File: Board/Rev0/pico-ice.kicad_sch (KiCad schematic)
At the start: 106 parts, among them J1 USB_C_Receptacle_USB2.0, J10 2x3_2.54mm_Female, J11 2x3_2.54mm_Female, J3 6X2 Female Header, J4 6X2 Female Header, J5 Conn_ARM_JTAG_SWD_10, J6 6X2 Female Header, J7 6X2 Female Header, J8 6X2 Female Header, J9 BOOT_SEL, SW1 PTS820 J25K SMTR LFS, SW2 PTS820 J25K SMTR LFS, U1 NCP1117ST33T3G, U2 W25Q32JVSSIQ, U3 RP2040, U4 CL9293A12L5M, U5 APS6404L-3SQN-SN, U6 ICE40UP5K-SG48ITR, U8 W25Q32JVSSIQ, Y1 12 MHz

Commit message: Updated the silkscreen layer
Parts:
- added LOGO1: tinyVS Logo, CUSTOM:tinyAI_logo, symbol MK11_PROG-rescue:TestPoint_Small-custom
- added LOGO2: WEEE Logo, CUSTOM:WEEE logo, symbol MK11_PROG-rescue:TestPoint_Small-custom
- added LOGO3: Pb free Logo, CUSTOM:Pb free logo, symbol MK11_PROG-rescue:TestPoint_Small-custom
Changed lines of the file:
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@@
     (pin "1")
+  )
+  (symbol (lib_id "MK11_PROG-rescue:TestPoint_Small-custom") (at 364.49 231.14 0) (unit 1)
+    (in_bom no) (on_board yes)
+    (property "Reference" "LOGO2" (id 0) (at 364.49 226.441 0))
+    (property "Value" "WEEE Logo" (id 1) (at 364.49 228.7524 0))
+    (property "Footprint" "CUSTOM:WEEE logo" (id 2) (at 369.57 231.14 0)
+      (effects (font (size 1.27 1.27)) hide)
+    )
+    (property "Datasheet" "~" (id 3) (at 369.57 231.14 0)
+      (effects (font (size 1.27 1.27)) hide)
+    )
+    (property "MPN" "DNP" (id 4) (at 364.49 231.14 0)
+      (effects (font (size 1.27 1.27)) hide)
+    )
+    (property "Digi-Key_PN" "DNP" (id 5) (at 364.49 231.14 0)
+      (effects (font (size 1.27 1.27)) hide)
+    )
+    (property "Manufacturer" "DNP" (id 6) (at 364.49 231.14 0)
+      (effects (font (size 1.27 1.27)) hide)
+    )
   )
   (symbol (lib_id "UPduino_v3.0:Device_R") (at 334.01 39.37 180) (unit 1)
@@
     (pin "4")
   )
+  (symbol (lib_id "MK11_PROG-rescue:TestPoint_Small-custom") (at 348.615 231.775 0) (unit 1)
+    (in_bom no) (on_board yes)
+    (property "Reference" "LOGO1" (id 0) (at 348.615 227.076 0))
+    (property "Value" "tinyVS Logo" (id 1) (at 348.615 229.3874 0))
+    (property "Footprint" "CUSTOM:tinyAI_logo" (id 2) (at 353.695 231.775 0)
+      (effects (font (size 1.27 1.27)) hide)
+    )
+    (property "Datasheet" "~" (id 3) (at 353.695 231.775 0)
+      (effects (font (size 1.27 1.27)) hide)
+    )
+    (property "MPN" "DNP" (id 4) (at 348.615 231.775 0)
+      (effects (font (size 1.27 1.27)) hide)
+    )
+    (property "Digi-Key_PN" "DNP" (id 5) (at 348.615 231.775 0)
+      (effects (font (size 1.27 1.27)) hide)
+    )
+    (property "Manufacturer" "DNP" (id 6) (at 348.615 231.775 0)
+      (effects (font (size 1.27 1.27)) hide)
+    )
+  )
   (symbol (lib_id "UPduino_v3.0:Device_R") (at 344.17 39.37 180) (unit 1)
     (in_bom yes) (on_board yes)
@@
     (pin "2")
   )
+  (symbol (lib_id "MK11_PROG-rescue:TestPoint_Small-custom") (at 378.46 231.14 0) (unit 1)
+    (in_bom no) (on_board yes)
+    (property "Reference" "LOGO3" (id 0) (at 378.46 226.441 0))
+    (property "Value" "Pb free Logo" (id 1) (at 378.46 228.7524 0))
+    (property "Footprint" "CUSTOM:Pb free logo" (id 2) (at 383.54 231.14 0)
+      (effects (font (size 1.27 1.27)) hide)
+    )
+    (property "Datasheet" "~" (id 3) (at 383.54 231.14 0)
+      (effects (font (size 1.27 1.27)) hide)
+    )
+    (property "MPN" "DNP" (id 4) (at 378.46 231.14 0)
+      (effects (font (size 1.27 1.27)) hide)
+    )
+    (property "Digi-Key_PN" "DNP" (id 5) (at 378.46 231.14 0)
+      (effects (font (size 1.27 1.27)) hide)
+    )
+    (property "Manufacturer" "DNP" (id 6) (at 378.46 231.14 0)
+      (effects (font (size 1.27 1.27)) hide)
+    )
+  )
   (symbol (lib_id "UPduino_v3.0:Device_C") (at 171.45 68.58 0) (unit 1)
     (in_bom yes) (on_board yes)
@@
       (reference "J11") (unit 1) (value "2x3_2.54mm_Female") (footprint "Connector_PinSocket_2.54mm:PinSocket_2x03_P2.54mm_Horizontal")
     )
+    (path "/802f85ef-6727-44b7-ba62-371a4e4b00b2"
+      (reference "LOGO1") (unit 1) (value "tinyVS Logo") (footprint "CUSTOM:tinyAI_logo")
+    )
+    (path "/2bb97fc1-2008-42b0-a4b8-60770020cee1"
+      (reference "LOGO2") (unit 1) (value "WEEE Logo") (footprint "CUSTOM:WEEE logo")
+    )
+    (path "/be4b6f0d-f662-4fd3-86e1-00a62d56607d"
+      (reference "LOGO3") (unit 1) (value "Pb free Logo") (footprint "CUSTOM:Pb free logo")
+    )
     (path "/049aa225-c9e7-467f-ab50-3f5e712805e5"

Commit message: Updated SCH/PCB
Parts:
- removed J5: Conn_ARM_JTAG_SWD_10, Connector_PinHeader_1.27mm:PinHeader_2x05_P1.27mm_Vertical_SMD, symbol Connector:Conn_ARM_JTAG_SWD_10
- added J2: SWD, Connector_PinHeader_2.54mm:PinHeader_1x02_P2.54mm_Vertical, symbol Connector_Generic:Conn_01x02
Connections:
- net SWCLK: now also J2.1 (Pin_1)
- net SWD: now also J2.2 (Pin_2)
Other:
- moved on the sheet: C8, J9, R2, R3, SW1, U2

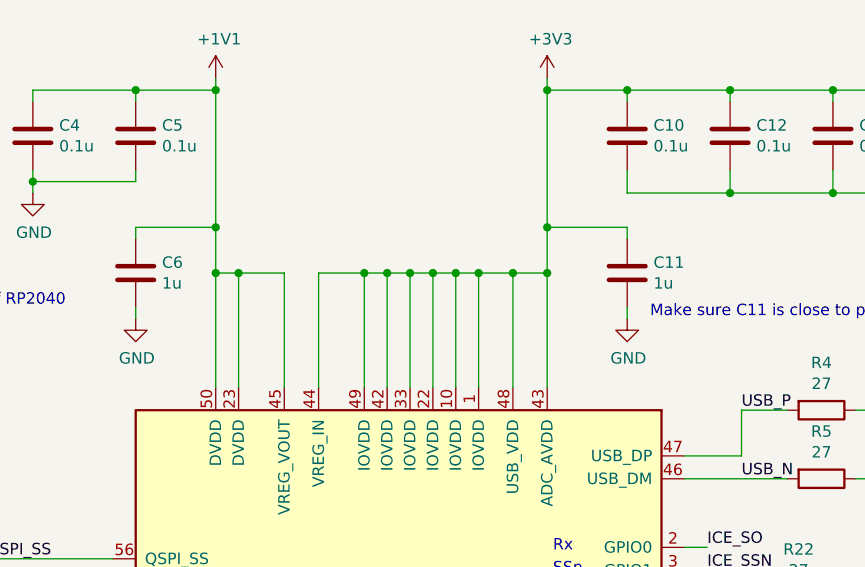
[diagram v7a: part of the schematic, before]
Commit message: Consolidated BoM (changed out 1uF to 4.7uF), generated gerbers and other output files
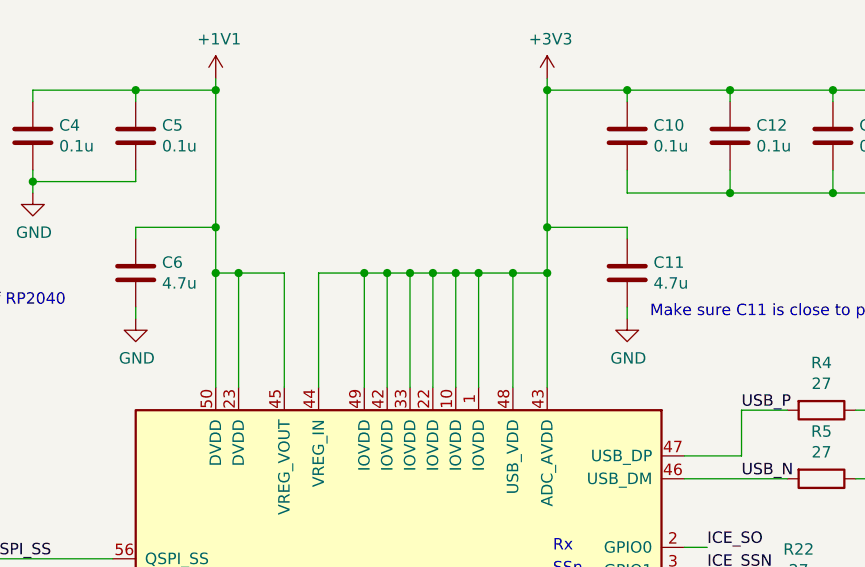
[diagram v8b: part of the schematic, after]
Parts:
- removed C11, C6: 1u, Capacitor_SMD:C_0402_1005Metric, symbol Device:C
- added C11, C6: 4.7u, Capacitor_SMD:C_0402_1005Metric, symbol UPduino_v3.0:Device_C
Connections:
- net +1V1: now also C6.1
- net +3V3: now also C11.1
- net GND: now also C11.2, C6.2
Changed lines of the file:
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@@
     (pin "1")
   )
-  (symbol (lib_id "Device:C") (at 59.69 83.82 0) (unit 1)
-    (in_bom yes) (on_board yes)
-    (property "Reference" "C6" (id 0) (at 62.611 82.6516 0)
-      (effects (font (size 1.27 1.27)) (justify left))
-    )
-    (property "Value" "1u" (id 1) (at 62.611 84.963 0)
-      (effects (font (size 1.27 1.27)) (justify left))
-    )
-    (property "Footprint" "Capacitor_SMD:C_0402_1005Metric" (id 2) (at 60.6552 87.63 0)
-      (effects (font (size 1.27 1.27)) hide)
-    )
-    (property "Datasheet" "~" (id 3) (at 59.69 83.82 0)
-      (effects (font (size 1.27 1.27)) hide)
-    )
-    (property "Description" "CAP CER 1UF 16V X5R 0402" (id 4) (at 59.69 83.82 0)
-      (effects (font (size 1.27 1.27)) hide)
-    )
-    (property "Digi-Key Part Number" "" (id 5) (at 59.69 83.82 0)
-      (effects (font (size 1.27 1.27)) hide)
-    )
-    (property "MPN" "EMK105BJ105KV-F" (id 6) (at 59.69 83.82 0)
-      (effects (font (size 1.27 1.27)) hide)
-    )
-    (property "Manufacturer" "Taiyo Yuden" (id 7) (at 59.69 83.82 0)
-      (effects (font (size 1.27 1.27)) hide)
-    )
-    (property "Supplier" "LCSC" (id 8) (at 59.69 83.82 0)
-      (effects (font (size 1.27 1.27)) hide)
-    )
-    (pin "1")
-    (pin "2")
-  )
-  (symbol (lib_id "Device:C") (at 114.3 83.82 0) (unit 1)
-    (in_bom yes) (on_board yes)
-    (property "Reference" "C11" (id 0) (at 117.221 82.6516 0)
-      (effects (font (size 1.27 1.27)) (justify left))
-    )
-    (property "Value" "1u" (id 1) (at 117.221 84.963 0)
-      (effects (font (size 1.27 1.27)) (justify left))
-    )
-    (property "Footprint" "Capacitor_SMD:C_0402_1005Metric" (id 2) (at 115.2652 87.63 0)
-      (effects (font (size 1.27 1.27)) hide)
-    )
-    (property "Datasheet" "~" (id 3) (at 114.3 83.82 0)
-      (effects (font (size 1.27 1.27)) hide)
-    )
-    (property "Description" "CAP CER 1UF 16V X5R 0402" (id 4) (at 114.3 83.82 0)
-      (effects (font (size 1.27 1.27)) hide)
-    )
-    (property "Digi-Key Part Number" "" (id 5) (at 114.3 83.82 0)
-      (effects (font (size 1.27 1.27)) hide)
-    )
-    (property "MPN" "EMK105BJ105KV-F" (id 6) (at 114.3 83.82 0)
-      (effects (font (size 1.27 1.27)) hide)
-    )
-    (property "Manufacturer" "Taiyo Yuden" (id 7) (at 114.3 83.82 0)
-      (effects (font (size 1.27 1.27)) hide)
-    )
-    (property "Supplier" "LCSC" (id 8) (at 114.3 83.82 0)
-      (effects (font (size 1.27 1.27)) hide)
-    )
-    (pin "1")
-    (pin "2")
-  )
   (symbol (lib_id "Mechanical:MountingHole") (at 283.845 266.065 0) (unit 1)
     (in_bom yes) (on_board yes)
@@
     (pin "1")
   )
+  (symbol (lib_id "UPduino_v3.0:Device_C") (at 59.69 83.82 0) (unit 1)
+    (in_bom yes) (on_board yes)
+    (property "Reference" "C6" (id 0) (at 62.611 82.6516 0)
+      (effects (font (size 1.27 1.27)) (justify left))
+    )
+    (property "Value" "4.7u" (id 1) (at 62.611 84.963 0)
+      (effects (font (size 1.27 1.27)) (justify left))
+    )
+    (property "Footprint" "Capacitor_SMD:C_0402_1005Metric" (id 2) (at 60.6552 87.63 0)
+      (effects (font (size 1.27 1.27)) hide)
+    )
+    (property "Datasheet" "~" (id 3) (at 59.69 83.82 0)
+      (effects (font (size 1.27 1.27)) hide)
+    )
+    (property "Description" "CAP CER 4.7UF 6.3V X5R 0402" (id 4) (at 59.69 83.82 0)
+      (effects (font (size 1.27 1.27)) hide)
+    )
+    (property "Digi-Key Part Number" "" (id 5) (at 59.69 83.82 0)
+      (effects (font (size 1.27 1.27)) hide)
+    )
+    (property "MPN" "GRM155R60J475ME87D" (id 6) (at 59.69 83.82 0)
+      (effects (font (size 1.27 1.27)) hide)
+    )
+    (property "Manufacturer" "Murata Electronics" (id 7) (at 59.69 83.82 0)
+      (effects (font (size 1.27 1.27)) hide)
+    )
+    (property "Supplier" "LCSC" (id 8) (at 59.69 83.82 0)
+      (effects (font (size 1.27 1.27)) hide)
+    )
+    (pin "1")
+    (pin "2")
+  )
   (symbol (lib_id "UPduino_v3.0:Device_C") (at 165.735 236.22 0) (mirror y) (unit 1)
     (in_bom yes) (on_board yes)
@@
     (pin "2")
   )
+  (symbol (lib_id "UPduino_v3.0:Device_C") (at 114.3 83.82 0) (unit 1)
+    (in_bom yes) (on_board yes)
+    (property "Reference" "C11" (id 0) (at 117.221 82.6516 0)
+      (effects (font (size 1.27 1.27)) (justify left))
+    )
+    (property "Value" "4.7u" (id 1) (at 117.221 84.963 0)
+      (effects (font (size 1.27 1.27)) (justify left))
+    )
+    (property "Footprint" "Capacitor_SMD:C_0402_1005Metric" (id 2) (at 115.2652 87.63 0)
+      (effects (font (size 1.27 1.27)) hide)
+    )
+    (property "Datasheet" "~" (id 3) (at 114.3 83.82 0)
+      (effects (font (size 1.27 1.27)) hide)
+    )
+    (property "Description" "CAP CER 4.7UF 6.3V X5R 0402" (id 4) (at 114.3 83.82 0)
+      (effects (font (size 1.27 1.27)) hide)
+    )
+    (property "Digi-Key Part Number" "" (id 5) (at 114.3 83.82 0)
+      (effects (font (size 1.27 1.27)) hide)
+    )
+    (property "MPN" "GRM155R60J475ME87D" (id 6) (at 114.3 83.82 0)
+      (effects (font (size 1.27 1.27)) hide)
+    )
+    (property "Manufacturer" "Murata Electronics" (id 7) (at 114.3 83.82 0)
+      (effects (font (size 1.27 1.27)) hide)
+    )
+    (property "Supplier" "LCSC" (id 8) (at 114.3 83.82 0)
+      (effects (font (size 1.27 1.27)) hide)
+    )
+    (pin "1")
+    (pin "2")
+  )
   (symbol (lib_id "UPduino_v3.0:Device_C") (at 160.02 68.58 0) (unit 1)
     (in_bom yes) (on_board yes)
@@
       (reference "C5") (unit 1) (value "0.1u") (footprint "Capacitor_SMD:C_0402_1005Metric")
     )
-    (path "/00000000-0000-0000-0000-00005ef07987"
-      (reference "C6") (unit 1) (value "1u") (footprint "Capacitor_SMD:C_0402_1005Metric")
+    (path "/7e6b9760-699e-4b36-a858-edf5ad884e6d"
+      (reference "C6") (unit 1) (value "4.7u") (footprint "Capacitor_SMD:C_0402_1005Metric")
     )
     (path "/9fb8d4da-8711-4525-a890-235cfadec771"
@@
       (reference "C10") (unit 1) (value "0.1u") (footprint "Capacitor_SMD:C_0402_1005Metric")
     )
-    (path "/00000000-0000-0000-0000-00005ef08170"
-      (reference "C11") (unit 1) (value "1u") (footprint "Capacitor_SMD:C_0402_1005Metric")
+    (path "/c2ca5cf7-6336-45d0-a16d-76389c79c6d9"
+      (reference "C11") (unit 1) (value "4.7u") (footprint "Capacitor_SMD:C_0402_1005Metric")
     )
     (path "/d223a1e0-a8be-4c92-a4f9-090079564686"
